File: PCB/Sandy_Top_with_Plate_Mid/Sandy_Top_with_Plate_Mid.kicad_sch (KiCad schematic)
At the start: 81 parts, among them J1 Conn_02x02_Top_Bottom, J2 Conn_02x02_Top_Bottom, J3 Conn_02x02_Top_Bottom

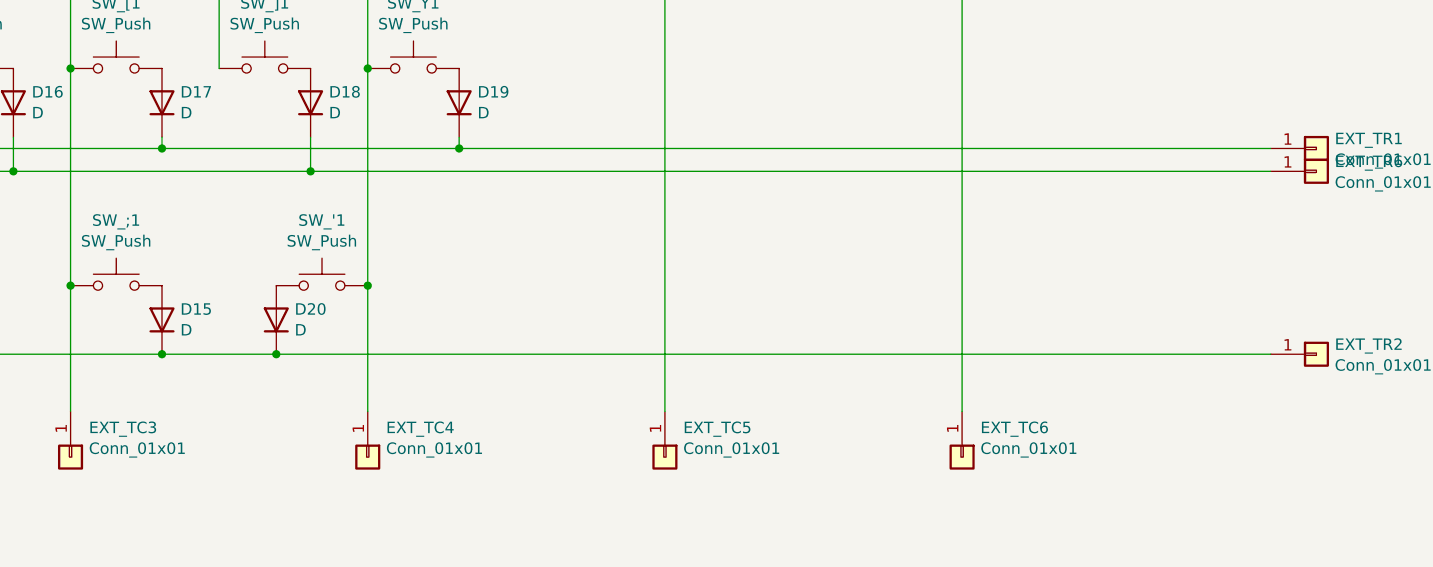
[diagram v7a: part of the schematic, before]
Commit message: シルクがハンダマスクに切り取られる箇所をフットプリントを変更して対応
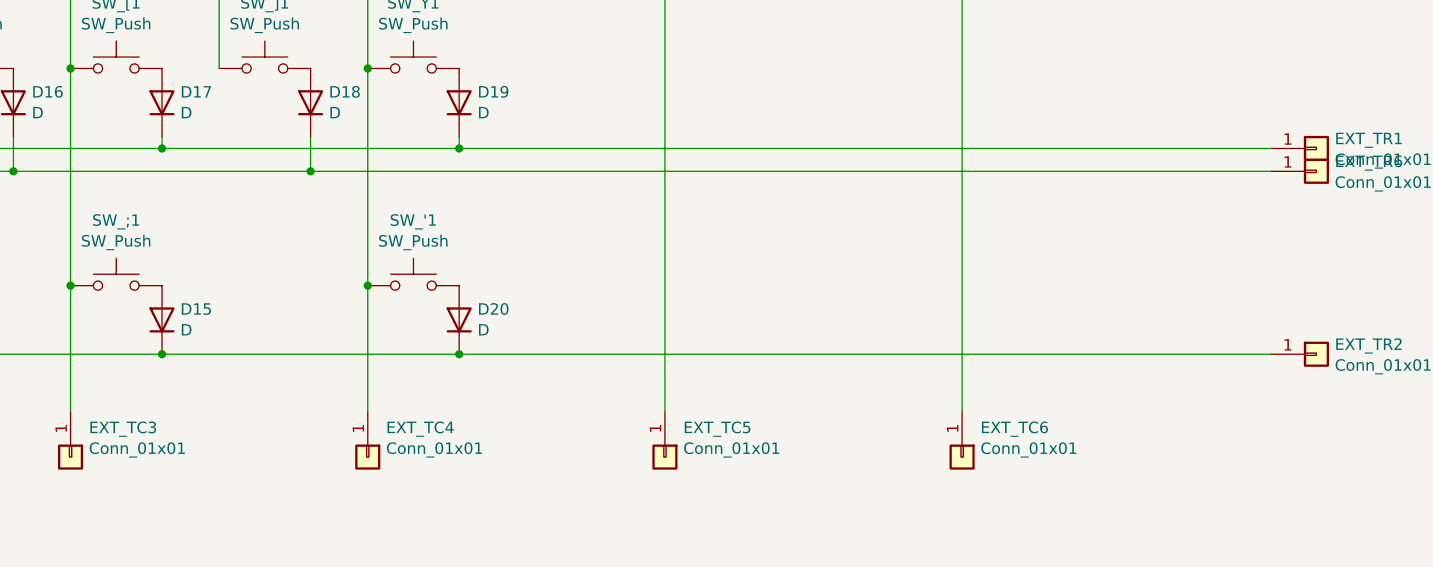
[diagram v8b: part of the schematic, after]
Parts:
- EXT_TC0, EXT_TC1, EXT_TC2, EXT_TC3, EXT_TC4, EXT_TC5, EXT_TC6, EXT_TR0, EXT_TR1, EXT_TR2, EXT_TR5, EXT_TR6: footprint TestPoint:TestPoint_THTPad_D2.0mm_Drill1.0mm -> locallib:TestPoint_THTPad_D2.0mm_Drill1.0mm
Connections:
- net Top_col4: now also SW_'1.1; no longer SW_'1.2
- net at D20.2 (A): now also SW_'1.2; no longer SW_'1.1
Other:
- moved on the sheet: D20, SW_'1
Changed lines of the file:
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@@
 	)
 	(junction
+		(at 171.45 93.345)
+		(diameter 0)
+		(color 0 0 0 0)
+	)
+	(junction
 		(at 98.425 208.28)
 		(diameter 0)
@@
 	)
 	(junction
-		(at 161.29 100.965)
-		(diameter 0)
-		(color 0 0 0 0)
-	)
-	(junction
 		(at 148.59 53.34)
 		(diameter 0)
@@
 	)
 	(junction
-		(at 171.45 93.345)
-		(diameter 0)
-		(color 0 0 0 0)
-	)
-	(junction
 		(at 154.94 44.45)
 		(diameter 0)
@@
 	)
 	(junction
+		(at 181.61 100.965)
+		(diameter 0)
+		(color 0 0 0 0)
+	)
+	(junction
 		(at 48.26 208.28)
 		(diameter 0)
@@
 	(wire
 		(pts
-			(xy 161.29 100.965) (xy 271.78 100.965)
-		)
-		(stroke
-			(width 0)
-			(type default)
-		)
-	)
-	(wire
-		(pts
 			(xy 90.805 255.27) (xy 88.265 255.27)
 		)
@@
 	(wire
 		(pts
-			(xy 171.45 69.215) (xy 171.45 93.345)
-		)
-		(stroke
-			(width 0)
-			(type default)
-		)
-	)
-	(wire
-		(pts
 			(xy 27.94 208.28) (xy 30.48 208.28)
 		)
@@
 	(wire
 		(pts
+			(xy 171.45 93.345) (xy 171.45 107.315)
+		)
+		(stroke
+			(width 0)
+			(type default)
+		)
+	)
+	(wire
+		(pts
 			(xy 83.185 227.33) (xy 98.425 208.28)
 		)
@@
 	(wire
 		(pts
-			(xy 148.59 100.965) (xy 161.29 100.965)
+			(xy 148.59 100.965) (xy 181.61 100.965)
 		)
 		(stroke
@@
 	(wire
 		(pts
+			(xy 181.61 100.965) (xy 271.78 100.965)
+		)
+		(stroke
+			(width 0)
+			(type default)
+		)
+	)
+	(wire
+		(pts
 			(xy 39.37 33.02) (xy 39.37 44.45)
 		)
@@
 	(wire
 		(pts
-			(xy 171.45 93.345) (xy 171.45 107.315)
+			(xy 171.45 69.215) (xy 171.45 93.345)
 		)
 		(stroke
@@
 			)
 		)
-		(property "Footprint" "TestPoint:TestPoint_THTPad_D2.0mm_Drill1.0mm"
+		(property "Footprint" "locallib:TestPoint_THTPad_D2.0mm_Drill1.0mm"
 			(at 171.45 112.395 0)
 			(effects
@@
 	(symbol
 		(lib_id "Switch:SW_Push")
-		(at 166.37 93.345 0)
+		(at 176.53 93.345 0)
 		(unit 1)
 		(exclude_from_sim no)
@@
 		(dnp no)
 		(property "Reference" "SW_'1"
-			(at 166.37 86.106 0)
+			(at 176.53 86.106 0)
 			(effects
 				(font
@@
 		)
 		(property "Value" "SW_Push"
-			(at 166.37 88.4174 0)
+			(at 176.53 88.4174 0)
 			(effects
 				(font
@@
 		)
 		(property "Footprint" "MX_Alps_Hybrid:MXOnly-1U-Hotswap-guide"
-			(at 166.37 88.265 0)
+			(at 176.53 88.265 0)
 			(effects
 				(font
@@
 		)
 		(property "Datasheet" "~"
-			(at 166.37 88.265 0)
+			(at 176.53 88.265 0)
 			(effects
 				(font
@@
 		)
 		(property "Description" ""
-			(at 166.37 93.345 0)
+			(at 176.53 93.345 0)
 			(effects
 				(font
@@
 			)
 		)
-		(property "Footprint" "TestPoint:TestPoint_THTPad_D2.0mm_Drill1.0mm"
+		(property "Footprint" "locallib:TestPoint_THTPad_D2.0mm_Drill1.0mm"
 			(at 237.49 112.395 0)
 			(effects
@@
 			)
 		)
-		(property "Footprint" "TestPoint:TestPoint_THTPad_D2.0mm_Drill1.0mm"
+		(property "Footprint" "locallib:TestPoint_THTPad_D2.0mm_Drill1.0mm"
 			(at 39.37 112.395 0)
 			(effects
@@
 			)
 		)
-		(property "Footprint" "TestPoint:TestPoint_THTPad_D2.0mm_Drill1.0mm"
+		(property "Footprint" "locallib:TestPoint_THTPad_D2.0mm_Drill1.0mm"
 			(at 276.86 53.34 0)
 			(effects
@@
 			)
 		)
-		(property "Footprint" "TestPoint:TestPoint_THTPad_D2.0mm_Drill1.0mm"
+		(property "Footprint" "locallib:TestPoint_THTPad_D2.0mm_Drill1.0mm"
 			(at 276.86 100.965 0)
 			(effects
@@
 			)
 		)
-		(property "Footprint" "TestPoint:TestPoint_THTPad_D2.0mm_Drill1.0mm"
+		(property "Footprint" "locallib:TestPoint_THTPad_D2.0mm_Drill1.0mm"
 			(at 276.86 55.88 0)
 			(effects
@@
 			)
 		)
-		(property "Footprint" "TestPoint:TestPoint_THTPad_D2.0mm_Drill1.0mm"
+		(property "Footprint" "locallib:TestPoint_THTPad_D2.0mm_Drill1.0mm"
 			(at 204.47 112.395 0)
 			(effects
@@
 			)
 		)
-		(property "Footprint" "TestPoint:TestPoint_THTPad_D2.0mm_Drill1.0mm"
+		(property "Footprint" "locallib:TestPoint_THTPad_D2.0mm_Drill1.0mm"
 			(at 105.41 112.395 0)
 			(effects
@@
 	(symbol
 		(lib_id "Device:D")
-		(at 161.29 97.155 90)
+		(at 181.61 97.155 90)
 		(unit 1)
 		(exclude_from_sim no)
@@
 		(dnp no)
 		(property "Reference" "D20"
-			(at 163.322 95.9866 90)
+			(at 183.642 95.9866 90)
 			(effects
 				(font
@@
 		)
 		(property "Value" "D"
-			(at 163.322 98.298 90)
+			(at 183.642 98.298 90)
 			(effects
 				(font
@@
 		)
 		(property "Footprint" "locallib:D_SOD-123_Emphasized_Direction_Line"
-			(at 161.29 97.155 0)
+			(at 181.61 97.155 0)
 			(effects
 				(font
@@
 		)
 		(property "Datasheet" "~"
-			(at 161.29 97.155 0)
+			(at 181.61 97.155 0)
 			(effects
 				(font
@@
 		)
 		(property "Description" ""
-			(at 161.29 97.155 0)
+			(at 181.61 97.155 0)
 			(effects
 				(font
@@
 		)
 		(property "LCSC" "C81598"
-			(at 161.29 97.155 0)
+			(at 181.61 97.155 0)
 			(effects
 				(font
@@
 		)
 		(property "Sim.Device" "D"
-			(at 161.29 97.155 0)
+			(at 181.61 97.155 0)
 			(effects
 				(font
@@
 		)
 		(property "Sim.Pins" "1=K 2=A"
-			(at 161.29 97.155 0)
+			(at 181.61 97.155 0)
 			(effects
 				(font
@@
 			)
 		)
-		(property "Footprint" "TestPoint:TestPoint_THTPad_D2.0mm_Drill1.0mm"
+		(property "Footprint" "locallib:TestPoint_THTPad_D2.0mm_Drill1.0mm"
 			(at 276.86 80.645 0)
 			(effects
@@
 			)
 		)
-		(property "Footprint" "TestPoint:TestPoint_THTPad_D2.0mm_Drill1.0mm"
+		(property "Footprint" "locallib:TestPoint_THTPad_D2.0mm_Drill1.0mm"
 			(at 138.43 112.395 0)
 			(effects
@@
 			)
 		)
-		(property "Footprint" "TestPoint:TestPoint_THTPad_D2.0mm_Drill1.0mm"
+		(property "Footprint" "locallib:TestPoint_THTPad_D2.0mm_Drill1.0mm"
 			(at 276.86 78.105 0)
 			(effects
@@
 			)
 		)
-		(property "Footprint" "TestPoint:TestPoint_THTPad_D2.0mm_Drill1.0mm"
+		(property "Footprint" "locallib:TestPoint_THTPad_D2.0mm_Drill1.0mm"
 			(at 72.39 112.395 0)
 			(effects
